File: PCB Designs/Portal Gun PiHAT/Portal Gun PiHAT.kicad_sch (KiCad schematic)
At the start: 6 parts, among them J1 GPIO, U1 CAT24C256

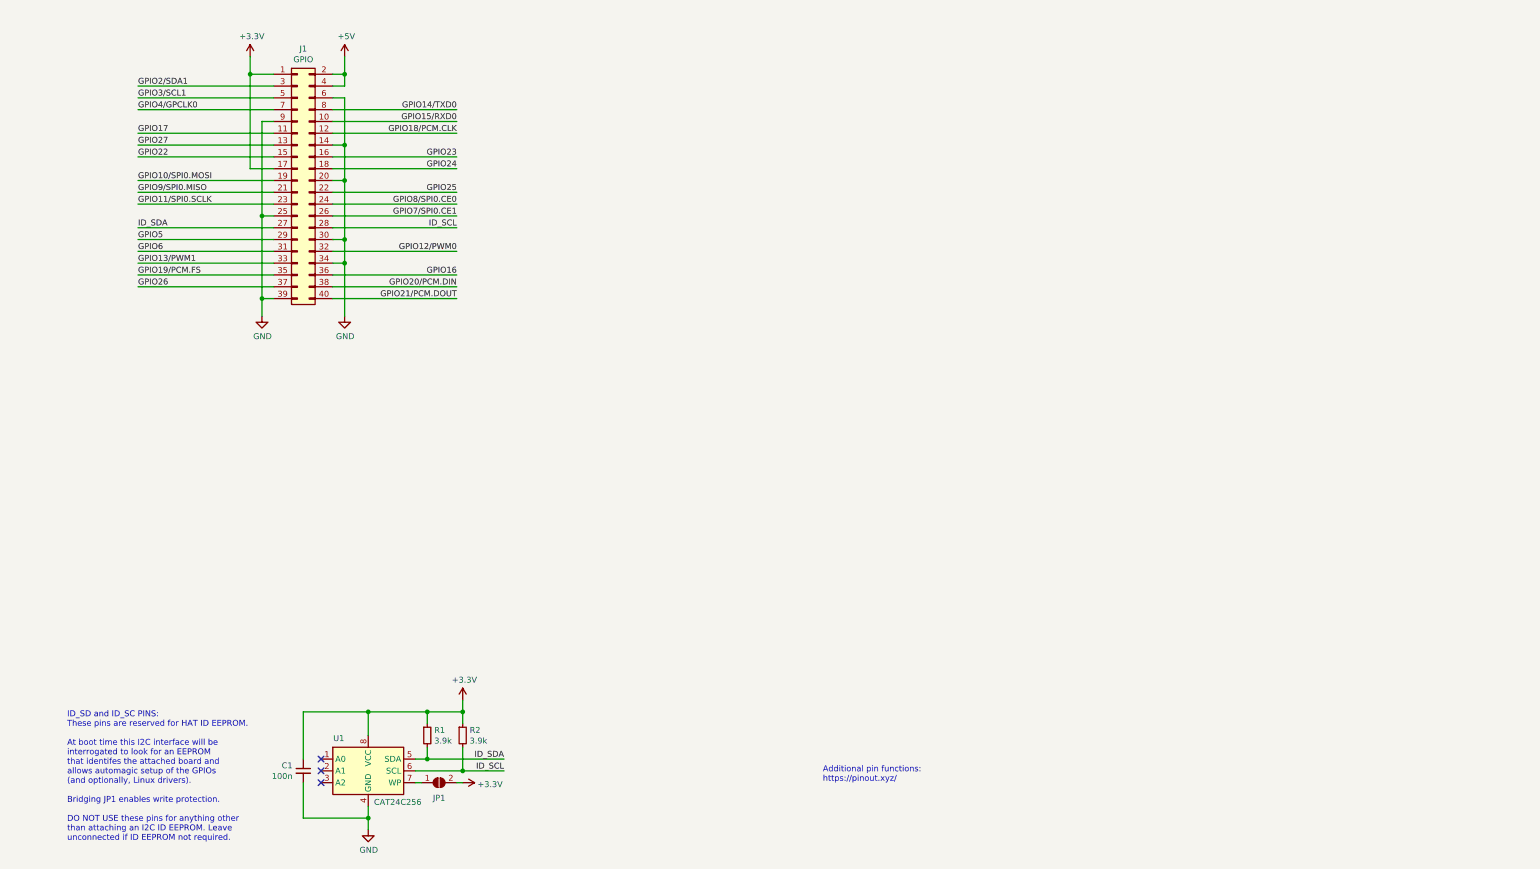
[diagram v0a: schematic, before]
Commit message: Added parts from prior kiKAD projects
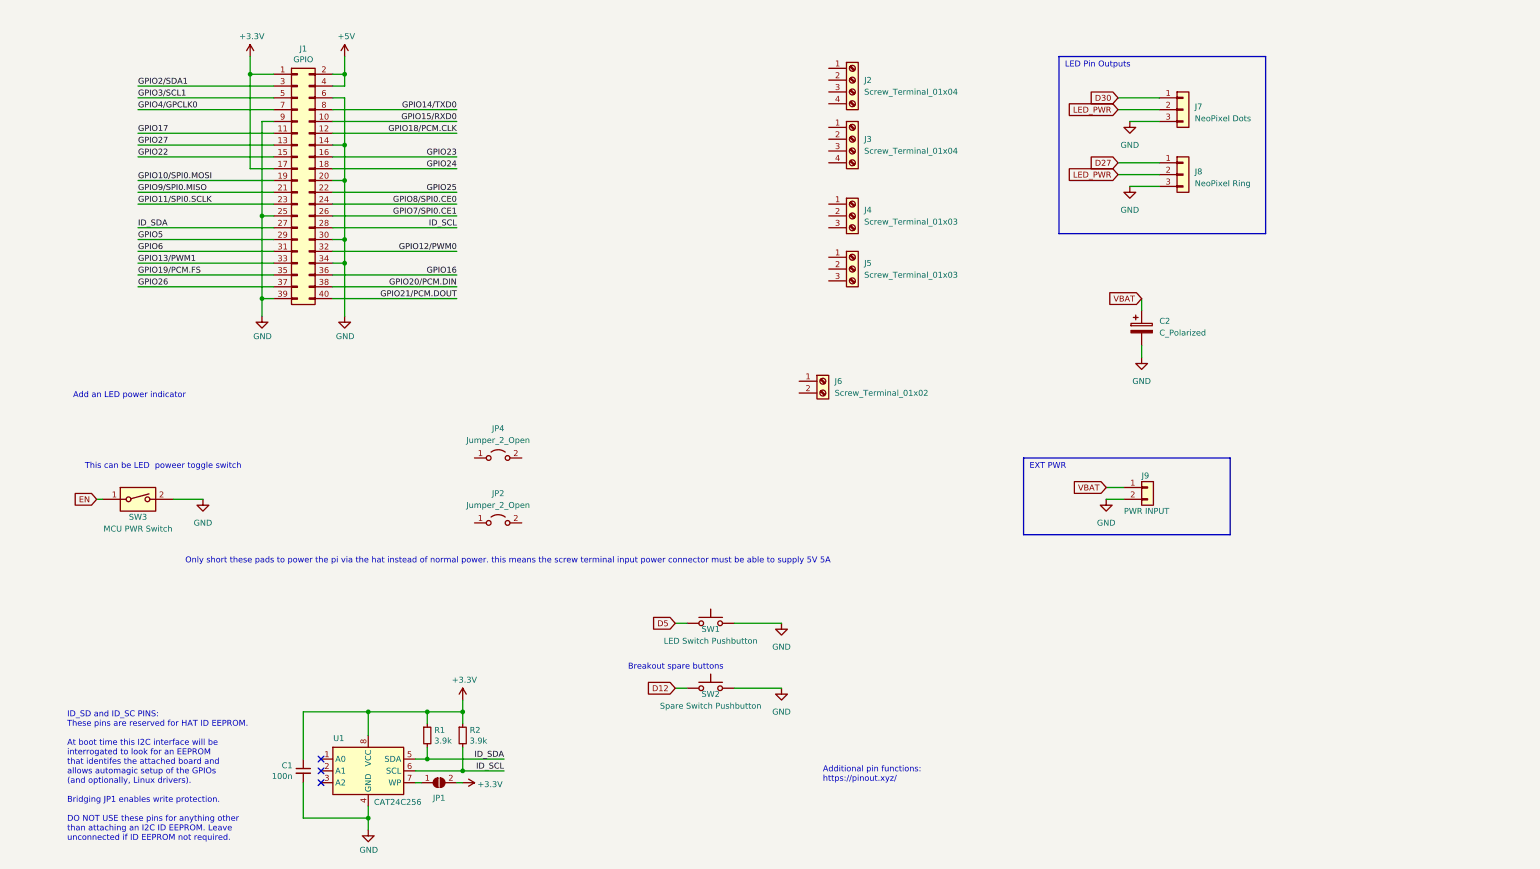
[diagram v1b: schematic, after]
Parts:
- added C2: C_Polarized, GrayFoxComponents:Horizontal Capacitor, symbol Device:C_Polarized
- added J2, J3: Screw_Terminal_01x04, symbol Connector:Screw_Terminal_01x04
- added J4, J5: Screw_Terminal_01x03, symbol Connector:Screw_Terminal_01x03
- added J6: Screw_Terminal_01x02, symbol Connector:Screw_Terminal_01x02
- added J7: NeoPixel Dots, Connector_PinHeader_2.54mm:PinHeader_1x03_P2.54mm_Vertical, symbol Connector_Generic:Conn_01x03
- added J8: NeoPixel Ring, Connector_PinHeader_2.54mm:PinHeader_1x03_P2.54mm_Vertical, symbol Connector_Generic:Conn_01x03
- added J9: PWR INPUT, Connector_PinSocket_2.54mm:PinSocket_1x02_P2.54mm_Vertical, symbol Connector_Generic:Conn_01x02
- added JP2, JP4: Jumper_2_Open, symbol Jumper:Jumper_2_Open
- added SW1: LED Switch Pushbutton, Connector_PinHeader_2.54mm:PinHeader_1x02_P2.54mm_Vertical, symbol Switch:SW_Push
- added SW2: Spare Switch Pushbutton, Connector_PinHeader_2.54mm:PinHeader_1x02_P2.54mm_Vertical, symbol Switch:SW_Push
- added SW3: MCU PWR Switch, Connector_PinHeader_2.54mm:PinHeader_1x02_P2.54mm_Vertical, symbol Switch:SW_DIP_x01
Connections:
- net GND: now also C2.2, J7.3 (Pin_3), J8.3 (Pin_3), J9.2 (Pin_2), SW1.2, SW2.2, SW3.2
- new net D12: SW2.1
- new net D27: J8.1 (Pin_1)
- new net D30: J7.1 (Pin_1)
- new net D5: SW1.1
- new net EN: SW3.1
- new net LED_PWR: J7.2 (Pin_2), J8.2 (Pin_2)
- new net VBAT: C2.1, J9.1 (Pin_1)
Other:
- note added: "Add an LED power indicator"
- note added: "Breakout spare buttons"
- note added: "EXT PWR"
- note added: "LED Pin Outputs"
- note added: "Only short these pads to power the pi via the hat instead of normal power. this means the screw terminal input power connector must be able to supply 5V 5A"
- note added: "This can be LED poweer toggle switch"

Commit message: schematic updates
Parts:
- removed J2, J3: Screw_Terminal_01x04, symbol Connector:Screw_Terminal_01x04
- removed J7: NeoPixel Dots, Connector_PinHeader_2.54mm:PinHeader_1x03_P2.54mm_Vertical, symbol Connector_Generic:Conn_01x03
- removed J8: NeoPixel Ring, Connector_PinHeader_2.54mm:PinHeader_1x03_P2.54mm_Vertical, symbol Connector_Generic:Conn_01x03
- removed J9: PWR INPUT, Connector_PinSocket_2.54mm:PinSocket_1x02_P2.54mm_Vertical, symbol Connector_Generic:Conn_01x02
- removed JP4: Jumper_2_Open, symbol Jumper:Jumper_2_Open
- added D1: 5V LED, symbol Device:LED
- added J2: SPARE_OUT_1, TerminalBlock_Phoenix:TerminalBlock_Phoenix_MKDS-1,5-2_1x02_P5.00mm_Horizontal, symbol Connector_Generic:Conn_01x02
- added J3: SPARE_OUT_2, TerminalBlock_Phoenix:TerminalBlock_Phoenix_MKDS-1,5-2_1x02_P5.00mm_Horizontal, symbol Connector_Generic:Conn_01x02
- added J7: PushButton2, symbol Connector:Screw_Terminal_01x04
- added J8: PushButton1, symbol Connector:Screw_Terminal_01x04
- added R3: 200ohm, symbol Device:R
- added R4, R5, R6, R7: 1kOhm, symbol Device:R
- added R8, R9: 300ohm, symbol Device:R
- C2: value C_Polarized -> 1000uF
- J4: value Screw_Terminal_01x03 -> NeoPixelFWD
- J5: value Screw_Terminal_01x03 -> NeoPixelAFT
- J6: value Screw_Terminal_01x02 -> 5V Input
- SW1: value LED Switch Pushbutton -> GPIO_SPARE_SW1
- SW2: value Spare Switch Pushbutton -> GPIO_SPARE_SW2
- SW3: value MCU PWR Switch -> LED_PWR_SW
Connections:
- net EN is gone; now on net +5V: SW3.1
- net GPIO27 is gone; now on net GPIO_SPARE_1: J1.13 (Pin_13)
- net GPIO2/SDA1 is gone; now on net GPIO_SPARE_2: J1.3 (Pin_3)
- net VBAT is gone; now on net VIN: C2.1
- net +3V3: now also J3.1 (Pin_1)
- net +5V: now also JP2.1 (A), J2.1 (Pin_1), J7.1 (Pin_1), J7.2 (Pin_2), J8.1 (Pin_1), J8.2 (Pin_2), R3.1
- net GND: now also J4.3 (Pin_3), J5.3 (Pin_3), J6.2 (Pin_2), D1.1 (K), J2.2 (Pin_2), J3.2 (Pin_2), J7.4 (Pin_4), J8.4 (Pin_4), R4.1, R5.1, R6.1, R7.1; no longer SW3.2
- net LED_PWR: now also J4.2 (Pin_2), J5.2 (Pin_2), SW3.2
- net VIN: now reaches JP2.2 (B)
- net VIN: now also J6.1 (Pin_1)
- net at J4.1 (Pin_1): now also R8.1
- net at J5.1 (Pin_1): now also R9.1
- net D12 renamed GPIO_SPARE_2
- net GPIO_SPARE_2: now also R7.2
- net D5 renamed GPIO_SPARE_1
- net GPIO_SPARE_1: now also R6.2
- net GPIO15/RXD0 renamed PB2_GPIO_WHT
- net PB2_GPIO_WHT: now also J7.3 (Pin_3), R5.2
- net GPIO17 renamed PB1_GPIO_WHT
- net PB1_GPIO_WHT: now also J8.3 (Pin_3), R4.2
- net GPIO18/PCM.CLK renamed LED_AFT_GPIO
- net LED_AFT_GPIO: now also R9.2
- net GPIO21/PCM.DOUT renamed LED_FWD_GPIO
- net LED_FWD_GPIO: now also R8.2
- new net: D1.2 (A), R3.2
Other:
- note added: "Adding a 300 to 500 Ohm resistor between your microcontroller's data pin and the data input on the first NeoPixel can help prevent voltage spikes that might otherwise damage your first pixel."
- note added: "EEPROM CONFIG"
- note added: "GPIO CONNECTOR"
- note added: "GPIO SPARES"
- note added: "LED PUSHBUTTONS"
- note added: "LED Power Indicator"
- note added: "NeoPixel Power Draw 2 Neopixels x 20mA / 1000 = 0.04A, @5V, 0.2W Min 2 Neopixels x 60mA / 1000 = 0.12A, @5V, 0.6W Max"
- note added: "Pin 1: LED RED Pin 2: COM YELLOW Pin 3: GPIO WHITE Pin 4: GND BLACK"
- note added: "Short these pads to power the pi via the hat instead of USB C. The screw terminal input power connector must be able to supply 5V 5A"
- note added: "This is used to switch the LEDs on/off. Short pins to bypass switch."
- note removed: "Add an LED power indicator"
- note removed: "Breakout spare buttons"
- note removed: "Only short these pads to power the pi via the hat instead of normal power. this means the screw terminal input power connector must be able to supply 5V 5A"
- note removed: "This can be LED poweer toggle switch"
- moved on the sheet: C2, J4, J5, J6, JP2, SW1, SW3

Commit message: KiCad PCBs Finalized
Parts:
- removed C1: 100n, symbol Device:C_Small
- removed JP1: ID_WP, symbol Jumper:SolderJumper_2_Open
- removed R1, R2: 3.9k, symbol Device:R_Small
- removed R8, R9: 300ohm, symbol Device:R
- removed U1: CAT24C256, symbol Memory_EEPROM:CAT24C256
- added J5: FAN_PWR, Connector_PinHeader_2.54mm:PinHeader_1x02_P2.54mm_Vertical, symbol Connector_Generic:Conn_01x02
- added TP1, TP2, TP3, TP4: TestPoint, TestPoint:TestPoint_Pad_D1.0mm, symbol Connector:TestPoint
- C1: renamed from C2; footprint GrayFoxComponents:Horizontal Capacitor -> Capacitor_THT:C_Radial_D10.0mm_H16.0mm_P5.00mm
- D1: footprint (none) -> LED_THT:LED_D3.0mm
- J1: renamed from J2; value SPARE_OUT_1 -> SPARE_5V_PWR; footprint TerminalBlock_Phoenix:TerminalBlock_Phoenix_MKDS-1,5-2_1x02_P5.00mm_Horizontal -> Connector_PinHeader_2.54mm:PinHeader_1x02_P2.54mm_Vertical
- J2: renamed from J6; footprint (none) -> TerminalBlock_Phoenix:TerminalBlock_Phoenix_MKDS-1,5-2_1x02_P5.00mm_Horizontal
- J4: renamed from J3; value SPARE_OUT_2 -> SPARE_3V_PWR; footprint TerminalBlock_Phoenix:TerminalBlock_Phoenix_MKDS-1,5-2_1x02_P5.00mm_Horizontal -> Connector_PinHeader_2.54mm:PinHeader_1x02_P2.54mm_Vertical
- J6: renamed from J4; footprint (none) -> TerminalBlock_Phoenix:TerminalBlock_Phoenix_MKDS-1,5-3_1x03_P5.00mm_Horizontal
- J7: renamed from J8; footprint (none) -> TerminalBlock_Phoenix:TerminalBlock_Phoenix_MKDS-1,5-4_1x04_P5.00mm_Horizontal
- J8: renamed from J7; footprint (none) -> TerminalBlock_Phoenix:TerminalBlock_Phoenix_MKDS-1,5-4_1x04_P5.00mm_Horizontal
- J9: renamed from J5; footprint (none) -> TerminalBlock_Phoenix:TerminalBlock_Phoenix_MKDS-1,5-3_1x03_P5.00mm_Horizontal
- JP1: renamed from JP2; footprint (none) -> Jumper:SolderJumper-2_P1.3mm_Open_Pad1.0x1.5mm
- R1: renamed from R6; footprint (none) -> Resistor_SMD:R_1206_3216Metric_Pad1.30x1.75mm_HandSolder
- R2: renamed from R7; footprint (none) -> Resistor_SMD:R_1206_3216Metric_Pad1.30x1.75mm_HandSolder
- R3, R4, R5: footprint (none) -> Resistor_SMD:R_1206_3216Metric_Pad1.30x1.75mm_HandSolder
- renumbered J1 to J3
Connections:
- net +3V3: now also TP2.1
- net +5V: now also J5.1 (Pin_1), TP1.1
- net GND: now also J5.2 (Pin_2), TP4.1
- net LED_AFT_GPIO: now also J9.1 (Pin_1)
- net LED_FWD_GPIO: now also J6.1 (Pin_1)
- net VIN: now also TP3.1
- no-connect marks 3 -> 22
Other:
- note added: "BLUE_PB"
- note added: "ORANGE_PB"
- note added: "Portal Gun Raspberry Pi Hat"
- note added: "TEST PADS"
- note removed: "Adding a 300 to 500 Ohm resistor between your microcontroller's data pin and the data input on the first NeoPixel can help prevent voltage spikes that might otherwise damage your first pixel."
- note removed: "Additional pin functions: https://pinout.xyz/"
- note removed: "EEPROM CONFIG"
- note removed: "ID_SD and ID_SC PINS: These pins are reserved for HAT ID EEPROM. At boot time this I2C interface will be interrogated to look for an EEPROM that identifes the attached board and allows automagic setup of the GPIOs (and optionally, Linux drivers). Bridging JP1 enables write protection. DO NOT USE these pins for anything other than attaching an I2C ID EEPROM. Leave unconnected if ID EEPROM not requ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"
- company: (none) -> Ranil Ganlath
- title: (none) -> Portal Gun Raspberry Pi Hat PCB
- moved on the sheet: C1, D1, J1, J2, J3, J4, J6, J7, J8, J9, JP1, R1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
